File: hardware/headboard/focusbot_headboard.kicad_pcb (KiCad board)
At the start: 2 copper layers, 46 x 30 mm, 12 parts

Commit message: fix(pcb): repair KiCad 10 syntax errors & feat(firmware): complete FocusBot v12.0 ESP32-S3 firmware
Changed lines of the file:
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@@
 		(layer "Edge.Cuts")
+	)
+	(gr_text "OPEN-SOURCE HARDWARE"
+		(at 150 94.8 0)
+		(layer "F.SilkS")
+		(effects
+			(font
+				(size 0.9 0.9)
+				(thickness 0.15)
+			)
+		)
+	)
+	(gr_text "FOCUSBOT HEADBOARD v12.0"
+		(at 150 92.5 0)
+		(layer "F.SilkS")
+		(effects
+			(font
+				(size 1.2 1.2)
+				(thickness 0.2)
+			)
+		)
 	)
 	(segment
@@
 	)
 	(embedded_fonts no)
-	(gr_text "FOCUSBOT HEADBOARD v12.0"
-		(at 150 92.5)
-		(layer "F.SilkS")
-		(uuid "fbc-hb-title-01")
-		(effects
-			(font
-				(size 1.2 1.2)
-				(thickness 0.2)
-			)
-			(justify center)
-		)
-	)
-	(gr_text "OPEN-SOURCE HARDWARE"
-		(at 150 94.8)
-		(layer "F.SilkS")
-		(uuid "fbc-hb-oshw-01")
-		(effects
-			(font
-				(size 0.8 0.8)
-				(thickness 0.15)
-			)
-			(justify center)
-		)
-	)
 )

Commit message: PCB: 0 DRC violations - fix 3V3 routing mainboard + clear headboard silkscreen overlaps
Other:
- board text removed: "FOCUSBOT HEADBOARD v12.0"
- board text removed: "OPEN-SOURCE HARDWARE"
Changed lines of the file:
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@@
 		(layer "Edge.Cuts")
-	)
-	(gr_text "OPEN-SOURCE HARDWARE"
-		(at 150 94.8 0)
-		(layer "F.SilkS")
-		(effects
-			(font
-				(size 0.9 0.9)
-				(thickness 0.15)
-			)
-		)
-	)
-	(gr_text "FOCUSBOT HEADBOARD v12.0"
-		(at 150 92.5 0)
-		(layer "F.SilkS")
-		(effects
-			(font
-				(size 1.2 1.2)
-				(thickness 0.2)
-			)
-		)
 	)
 	(segment

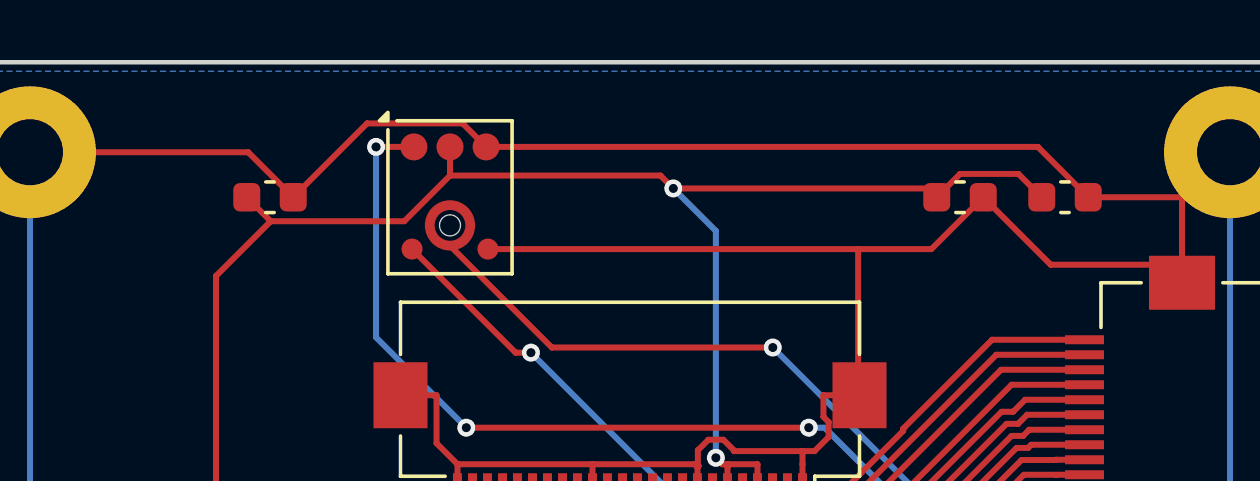
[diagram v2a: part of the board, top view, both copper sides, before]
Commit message: feat(branding): rename project to FocusBot, clean up CAD/KiCad artifacts, add photorealistic 3D renders to README
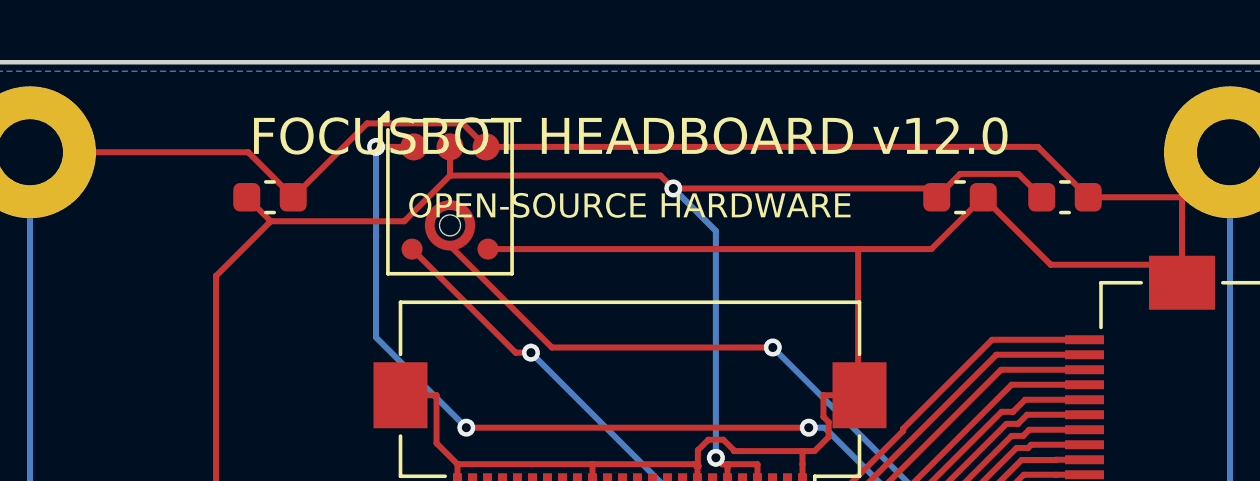
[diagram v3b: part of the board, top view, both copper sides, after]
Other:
- board text added: "FOCUSBOT HEADBOARD v12.0"
- board text added: "OPEN-SOURCE HARDWARE"
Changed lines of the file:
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@@
 	)
 	(embedded_fonts no)
+	(gr_text "FOCUSBOT HEADBOARD v12.0"
+		(at 150 92.5)
+		(layer "F.SilkS")
+		(uuid "fbc-hb-title-01")
+		(effects
+			(font
+				(size 1.2 1.2)
+				(thickness 0.2)
+			)
+			(justify center)
+		)
+	)
+	(gr_text "OPEN-SOURCE HARDWARE"
+		(at 150 94.8)
+		(layer "F.SilkS")
+		(uuid "fbc-hb-oshw-01")
+		(effects
+			(font
+				(size 0.8 0.8)
+				(thickness 0.15)
+			)
+			(justify center)
+		)
+	)
 )
